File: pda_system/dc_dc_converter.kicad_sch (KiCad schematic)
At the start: 15 parts

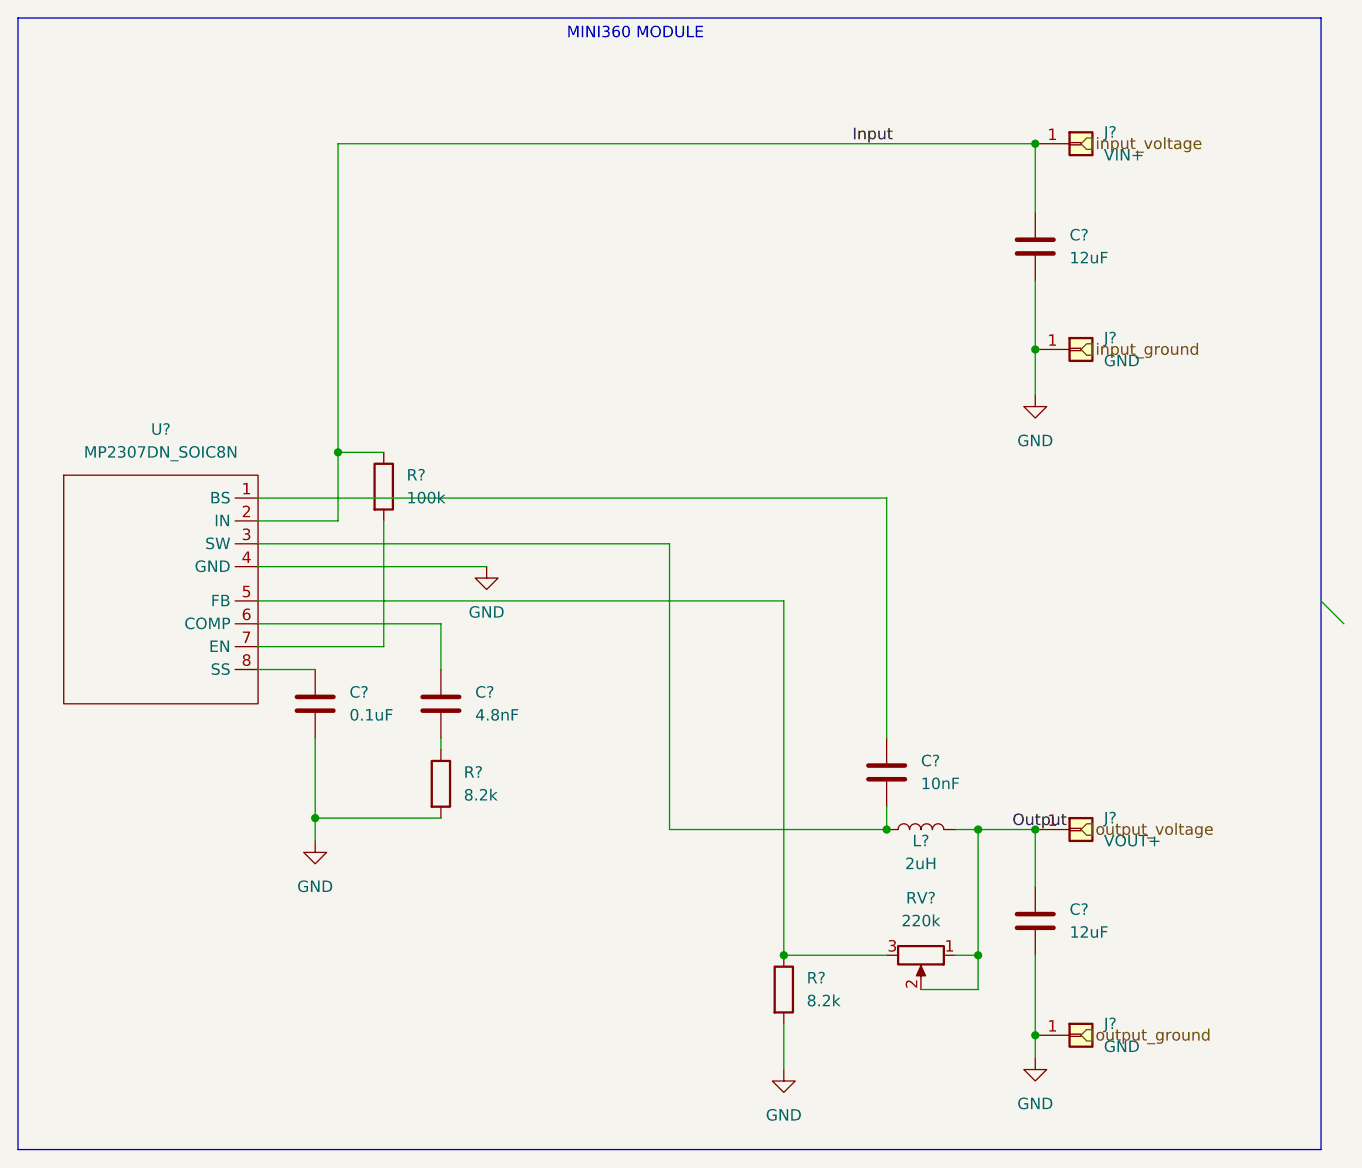
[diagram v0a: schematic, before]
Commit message: updated the network labels along with global nets. Also added programming/debugging port to schematic.
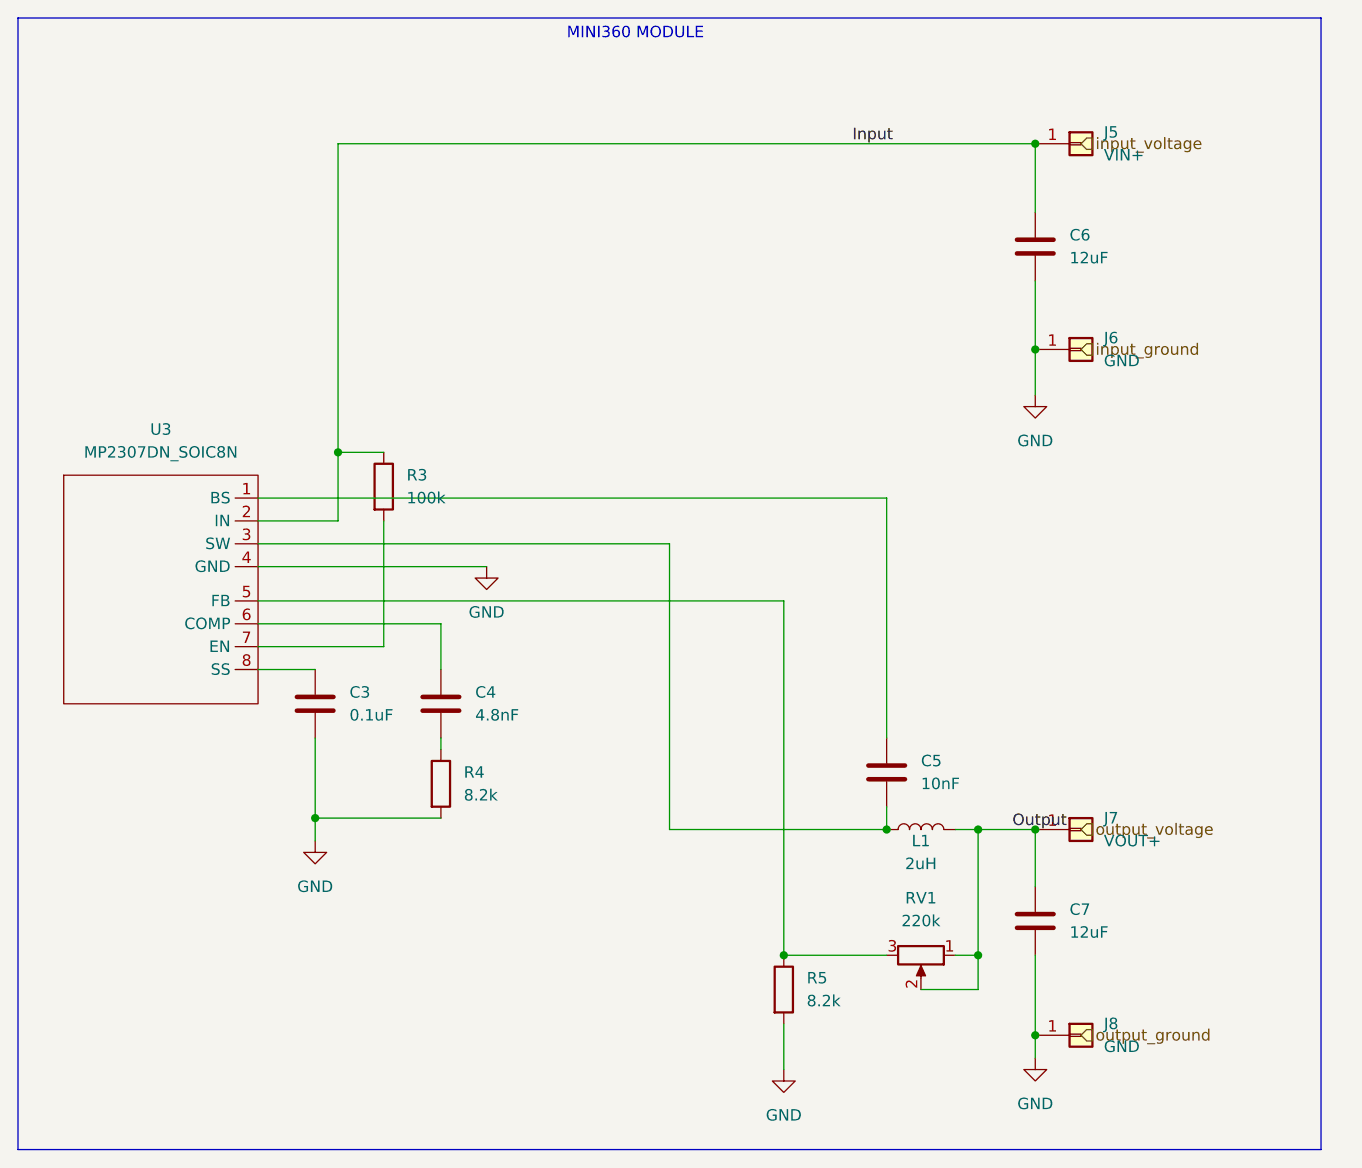
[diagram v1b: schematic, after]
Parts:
- gave numbers to parts that had none: 15
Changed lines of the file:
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@@
   (junction (at 133.35 115.57) (diameter 0) (color 0 0 0 0)
-  )
-  (bus_entry (at 165.1 90.17) (size 2.54 2.54)
-    (stroke (width 0) (type default) (color 0 0 0 0))
   )
   (wire (pts (xy 124.46 115.57) (xy 127 115.57))
@@
   (symbol (lib_id "Device:R") (at 60.96 77.47 0) (unit 1)
     (in_bom yes) (on_board yes) (fields_autoplaced)
-    (property "Reference" "R?" (id 0) (at 63.5 76.1999 0)
+    (property "Reference" "R3" (id 0) (at 63.5 76.1999 0)
       (effects (font (size 1.27 1.27)) (justify left))
     )
@@
   (symbol (lib_id "Device:R") (at 67.31 110.49 0) (unit 1)
     (in_bom yes) (on_board yes) (fields_autoplaced)
-    (property "Reference" "R?" (id 0) (at 69.85 109.2199 0)
+    (property "Reference" "R4" (id 0) (at 69.85 109.2199 0)
       (effects (font (size 1.27 1.27)) (justify left))
     )
@@
   (symbol (lib_id "Connector_Generic:Conn_01x01") (at 138.43 138.43 0) (unit 1)
     (in_bom yes) (on_board yes) (fields_autoplaced)
-    (property "Reference" "J?" (id 0) (at 140.97 137.1599 0)
+    (property "Reference" "J8" (id 0) (at 140.97 137.1599 0)
       (effects (font (size 1.27 1.27)) (justify left))
     )
@@
   (symbol (lib_id "Device:C") (at 116.84 109.22 0) (unit 1)
     (in_bom yes) (on_board yes) (fields_autoplaced)
-    (property "Reference" "C?" (id 0) (at 120.65 107.9499 0)
+    (property "Reference" "C5" (id 0) (at 120.65 107.9499 0)
       (effects (font (size 1.27 1.27)) (justify left))
     )
@@
   (symbol (lib_id "Device:C") (at 133.35 50.8 0) (unit 1)
     (in_bom yes) (on_board yes) (fields_autoplaced)
-    (property "Reference" "C?" (id 0) (at 137.16 49.5299 0)
+    (property "Reference" "C6" (id 0) (at 137.16 49.5299 0)
       (effects (font (size 1.27 1.27)) (justify left))
     )
@@
   (symbol (lib_id "Connector_Generic:Conn_01x01") (at 138.43 62.23 0) (unit 1)
     (in_bom yes) (on_board yes) (fields_autoplaced)
-    (property "Reference" "J?" (id 0) (at 140.97 60.9599 0)
+    (property "Reference" "J6" (id 0) (at 140.97 60.9599 0)
       (effects (font (size 1.27 1.27)) (justify left))
     )
@@
   (symbol (lib_id "Device:R") (at 105.41 133.35 0) (unit 1)
     (in_bom yes) (on_board yes) (fields_autoplaced)
-    (property "Reference" "R?" (id 0) (at 107.95 132.0799 0)
+    (property "Reference" "R5" (id 0) (at 107.95 132.0799 0)
       (effects (font (size 1.27 1.27)) (justify left))
     )
@@
   (symbol (lib_id "Device:R_Potentiometer") (at 120.65 129.54 270) (unit 1)
     (in_bom yes) (on_board yes) (fields_autoplaced)
-    (property "Reference" "RV?" (id 0) (at 120.65 123.19 90))
+    (property "Reference" "RV1" (id 0) (at 120.65 123.19 90))
     (property "Value" "220k" (id 1) (at 120.65 125.73 90))
     (property "Footprint" "" (id 2) (at 120.65 129.54 0)
@@
   (symbol (lib_id "Connector_Generic:Conn_01x01") (at 138.43 115.57 0) (unit 1)
     (in_bom yes) (on_board yes) (fields_autoplaced)
-    (property "Reference" "J?" (id 0) (at 140.97 114.2999 0)
+    (property "Reference" "J7" (id 0) (at 140.97 114.2999 0)
       (effects (font (size 1.27 1.27)) (justify left))
     )
@@
   (symbol (lib_id "Device:C") (at 133.35 125.73 0) (unit 1)
     (in_bom yes) (on_board yes) (fields_autoplaced)
-    (property "Reference" "C?" (id 0) (at 137.16 124.4599 0)
+    (property "Reference" "C7" (id 0) (at 137.16 124.4599 0)
       (effects (font (size 1.27 1.27)) (justify left))
     )
@@
   (symbol (lib_id "Device:L") (at 120.65 115.57 90) (unit 1)
     (in_bom yes) (on_board yes)
-    (property "Reference" "L?" (id 0) (at 120.65 116.84 90))
+    (property "Reference" "L1" (id 0) (at 120.65 116.84 90))
     (property "Value" "2uH" (id 1) (at 120.65 119.38 90))
     (property "Footprint" "" (id 2) (at 120.65 115.57 0)
@@
   (symbol (lib_id "Device:C") (at 67.31 101.6 0) (unit 1)
     (in_bom yes) (on_board yes) (fields_autoplaced)
-    (property "Reference" "C?" (id 0) (at 71.12 100.3299 0)
+    (property "Reference" "C4" (id 0) (at 71.12 100.3299 0)
       (effects (font (size 1.27 1.27)) (justify left))
     )
@@
   (symbol (lib_id "Device:C") (at 53.34 101.6 0) (unit 1)
     (in_bom yes) (on_board yes) (fields_autoplaced)
-    (property "Reference" "C?" (id 0) (at 57.15 100.3299 0)
+    (property "Reference" "C3" (id 0) (at 57.15 100.3299 0)
       (effects (font (size 1.27 1.27)) (justify left))
     )
@@
   (symbol (lib_id "pda_system_lib:MP2307DN_SOIC8N") (at 35.56 85.09 0) (unit 1)
     (in_bom yes) (on_board yes) (fields_autoplaced)
-    (property "Reference" "U?" (id 0) (at 36.195 71.12 0))
+    (property "Reference" "U3" (id 0) (at 36.195 71.12 0))
     (property "Value" "MP2307DN_SOIC8N" (id 1) (at 36.195 73.66 0))
     (property "Footprint" "Package_SO:SOIC-8-1EP_3.9x4.9mm_P1.27mm_EP2.29x3mm" (id 2) (at 35.56 85.09 0)
@@
   (symbol (lib_id "Connector_Generic:Conn_01x01") (at 138.43 39.37 0) (unit 1)
     (in_bom yes) (on_board yes) (fields_autoplaced)
-    (property "Reference" "J?" (id 0) (at 140.97 38.0999 0)
-      (effects (font (size 1.27 1.27)) (justify left))
-    )
+    (property "Reference" "J5" (id 0) (at 140.97 38.0999 0)
+      (effects (font (size 1.27 1.27)) (justify left))
+    )

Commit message: fixed some connection issues, and imported the bluepill module
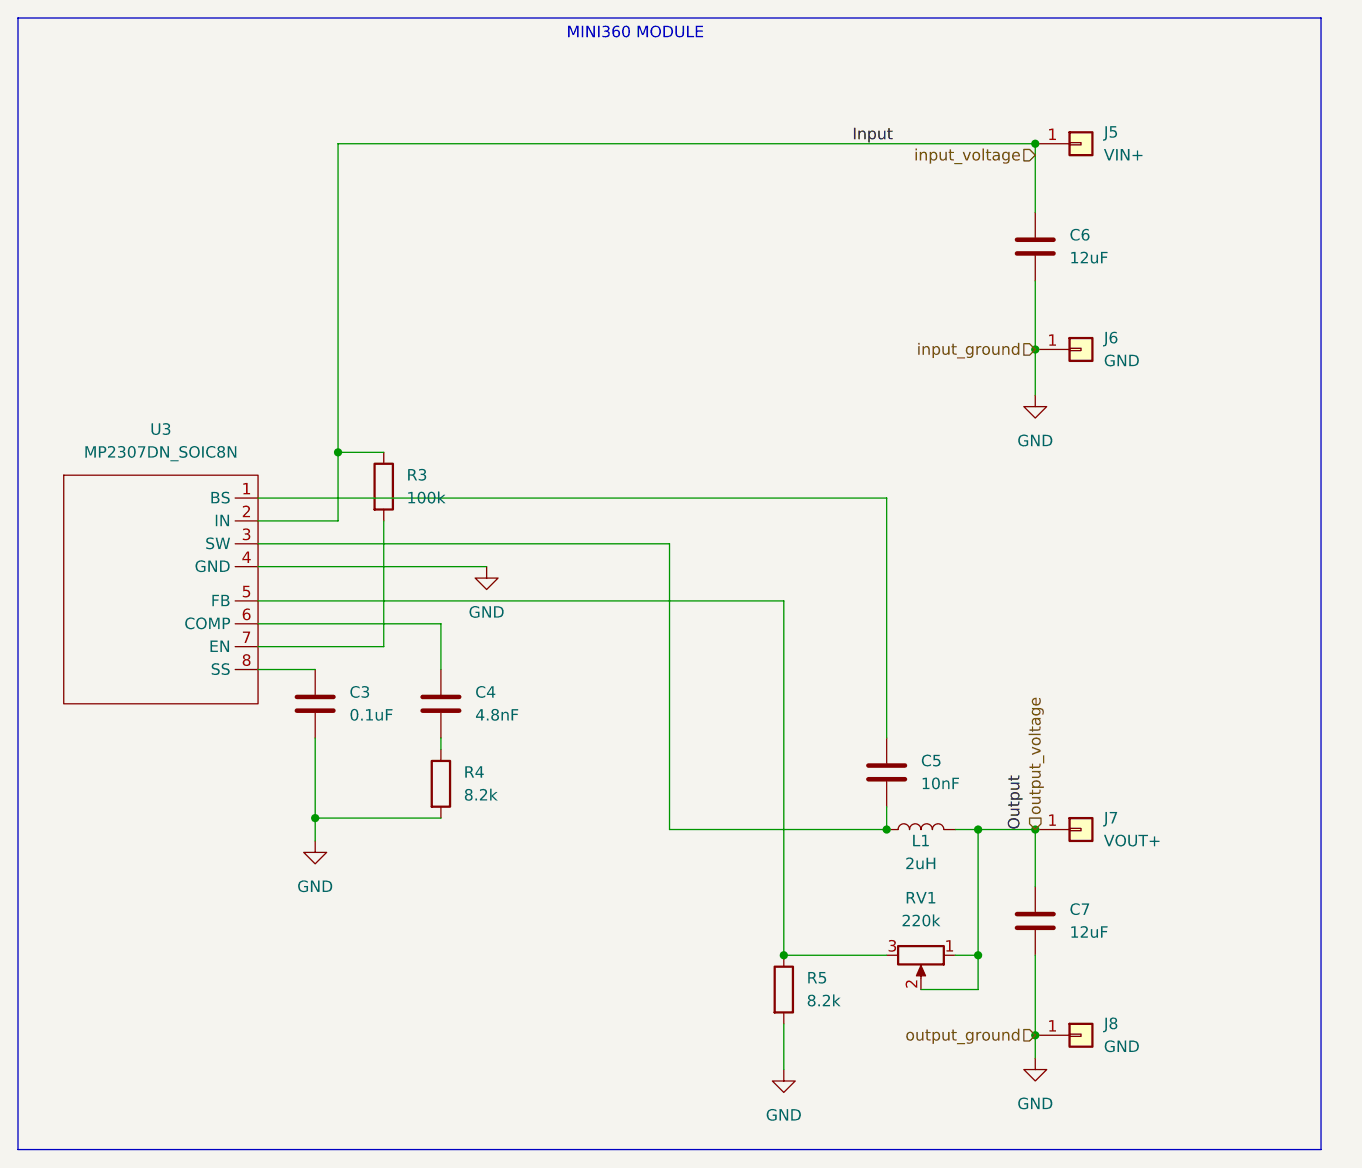
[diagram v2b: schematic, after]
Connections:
- net Input is gone; now on net input_voltage: C6.1, J5.1 (Pin_1), R3.1, U3.2 (IN)
- net Output is gone; now on net output_voltage: C7.1, J7.1 (Pin_1), L1.2, RV1.1, RV1.2
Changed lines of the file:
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@@
     (effects (font (size 1.27 1.27)) (justify left bottom))
   )
-  (label "Output" (at 130.81 115.57 0)
+  (label "Output" (at 132.08 115.57 90)
     (effects (font (size 1.27 1.27)) (justify left bottom))
   )
-  (hierarchical_label "input_ground" (shape input) (at 138.43 62.23 0)
+  (hierarchical_label "input_ground" (shape input) (at 133.35 62.23 180)
+    (effects (font (size 1.27 1.27)) (justify right))
+  )
+  (hierarchical_label "output_ground" (shape input) (at 133.35 138.43 180)
+    (effects (font (size 1.27 1.27)) (justify right))
+  )
+  (hierarchical_label "output_voltage" (shape input) (at 133.35 115.57 90)
     (effects (font (size 1.27 1.27)) (justify left))
   )
-  (hierarchical_label "output_ground" (shape input) (at 138.43 138.43 0)
-    (effects (font (size 1.27 1.27)) (justify left))
-  )
-  (hierarchical_label "output_voltage" (shape input) (at 138.43 115.57 0)
-    (effects (font (size 1.27 1.27)) (justify left))
-  )
-  (hierarchical_label "input_voltage" (shape input) (at 138.43 39.37 0)
-    (effects (font (size 1.27 1.27)) (justify left))
+  (hierarchical_label "input_voltage" (shape input) (at 133.35 40.64 180)
+    (effects (font (size 1.27 1.27)) (justify right))
   )
   (symbol (lib_id "Device:R") (at 60.96 77.47 0) (unit 1)

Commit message: fixed two more errors with electrical rules check
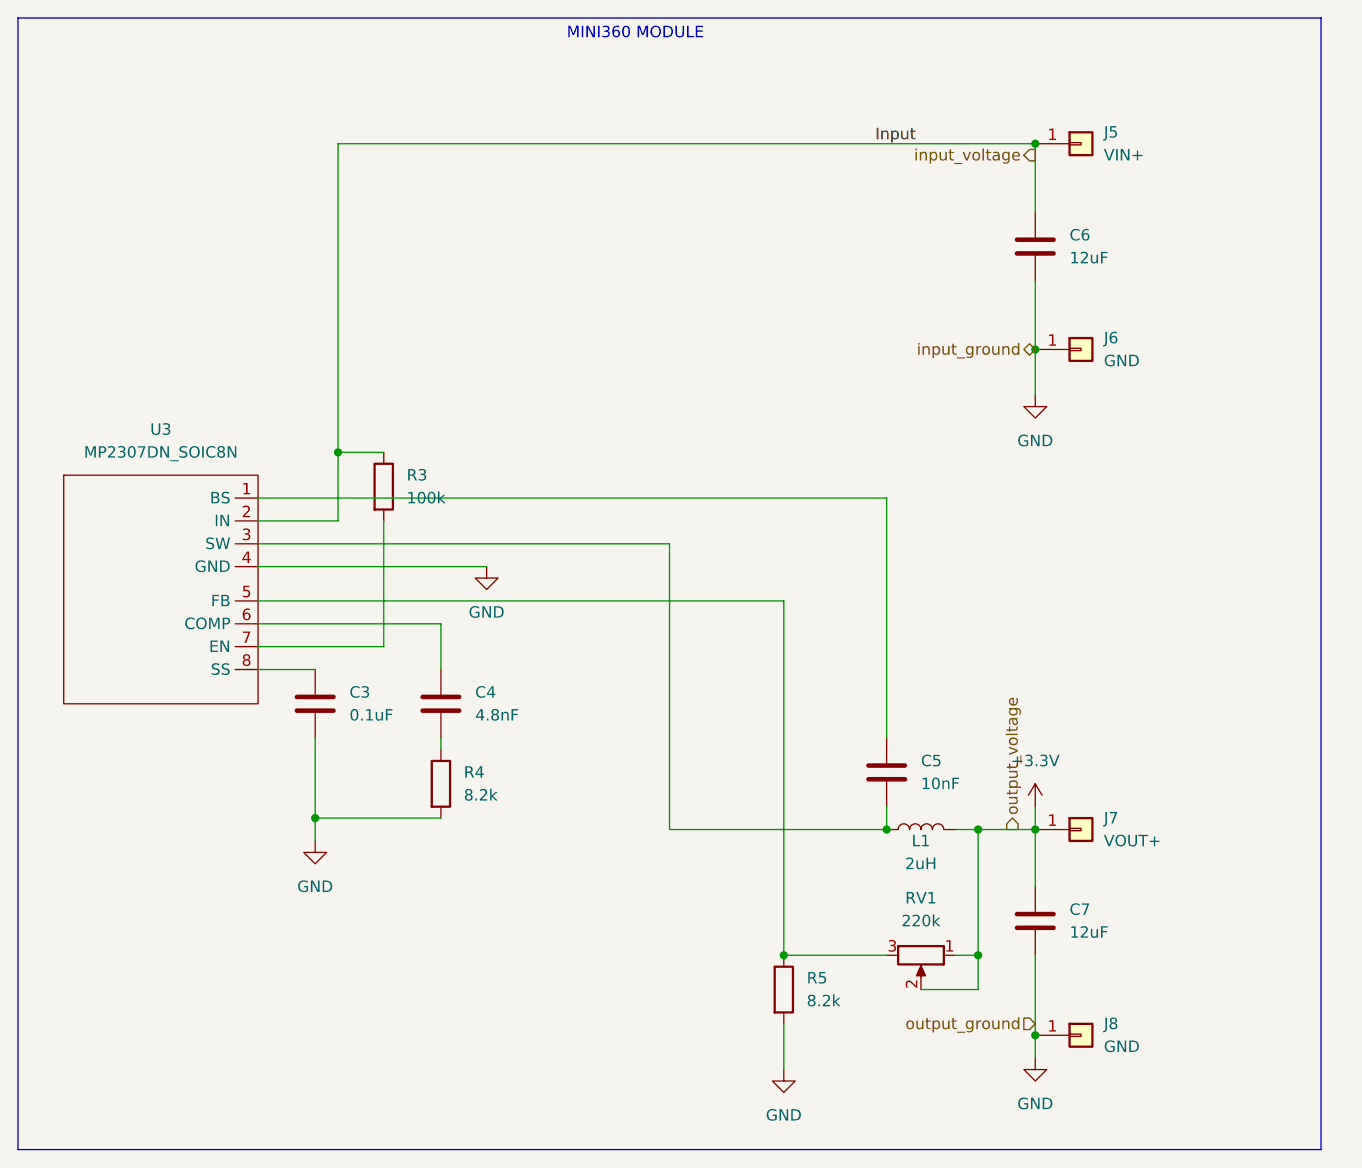
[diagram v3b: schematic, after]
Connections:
- net output_voltage renamed +3V3
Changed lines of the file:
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@@
+    (stroke (width 0) (type default) (color 0 0 0 0))
+  )
+  (wire (pts (xy 133.35 113.03) (xy 133.35 115.57))
     (stroke (width 0) (type default) (color 0 0 0 0))
   )
@@
     (effects (font (size 1.27 1.27)) (justify left bottom))
   )
-  (label "Input" (at 113.03 39.37 0)
+  (label "Input" (at 115.57 39.37 0)
     (effects (font (size 1.27 1.27)) (justify left bottom))
   )
-  (label "Output" (at 132.08 115.57 90)
-    (effects (font (size 1.27 1.27)) (justify left bottom))
-  )
-  (hierarchical_label "input_ground" (shape input) (at 133.35 62.23 180)
+  (hierarchical_label "input_ground" (shape bidirectional) (at 133.35 62.23 180)
     (effects (font (size 1.27 1.27)) (justify right))
   )
-  (hierarchical_label "output_ground" (shape input) (at 133.35 138.43 180)
+  (hierarchical_label "output_ground" (shape input) (at 133.35 137.16 180)
     (effects (font (size 1.27 1.27)) (justify right))
   )
-  (hierarchical_label "output_voltage" (shape input) (at 133.35 115.57 90)
+  (hierarchical_label "output_voltage" (shape output) (at 130.81 115.57 90)
     (effects (font (size 1.27 1.27)) (justify left))
   )
-  (hierarchical_label "input_voltage" (shape input) (at 133.35 40.64 180)
+  (hierarchical_label "input_voltage" (shape output) (at 133.35 40.64 180)
     (effects (font (size 1.27 1.27)) (justify right))
   )
@@
       (effects (font (size 1.27 1.27)) hide)
     )
+    (pin "1")
+  )
+  (symbol (lib_id "power:+3.3V") (at 133.35 113.03 0) (unit 1)
+    (in_bom yes) (on_board yes) (fields_autoplaced)
+    (property "Reference" "#PWR0110" (id 0) (at 133.35 116.84 0)
+      (effects (font (size 1.27 1.27)) hide)
+    )
+    (property "Value" "+3.3V" (id 1) (at 133.35 107.95 0))
+    (property "Footprint" "" (id 2) (at 133.35 113.03 0)
+      (effects (font (size 1.27 1.27)) hide)
+    )
+    (property "Datasheet" "" (id 3) (at 133.35 113.03 0)
+      (effects (font (size 1.27 1.27)) hide)
+    )
